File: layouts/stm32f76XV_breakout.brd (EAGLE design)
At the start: 35.6 x 44.5 mm, 52 parts, among them J1 FTSH-105-01-F-DV-K, K1 USB-MICROZX62R-B, K2 MICRO_SD01, Q1 25 MHz, T2 FDC5614P, U3 LMZ21701, U5 NUF2221

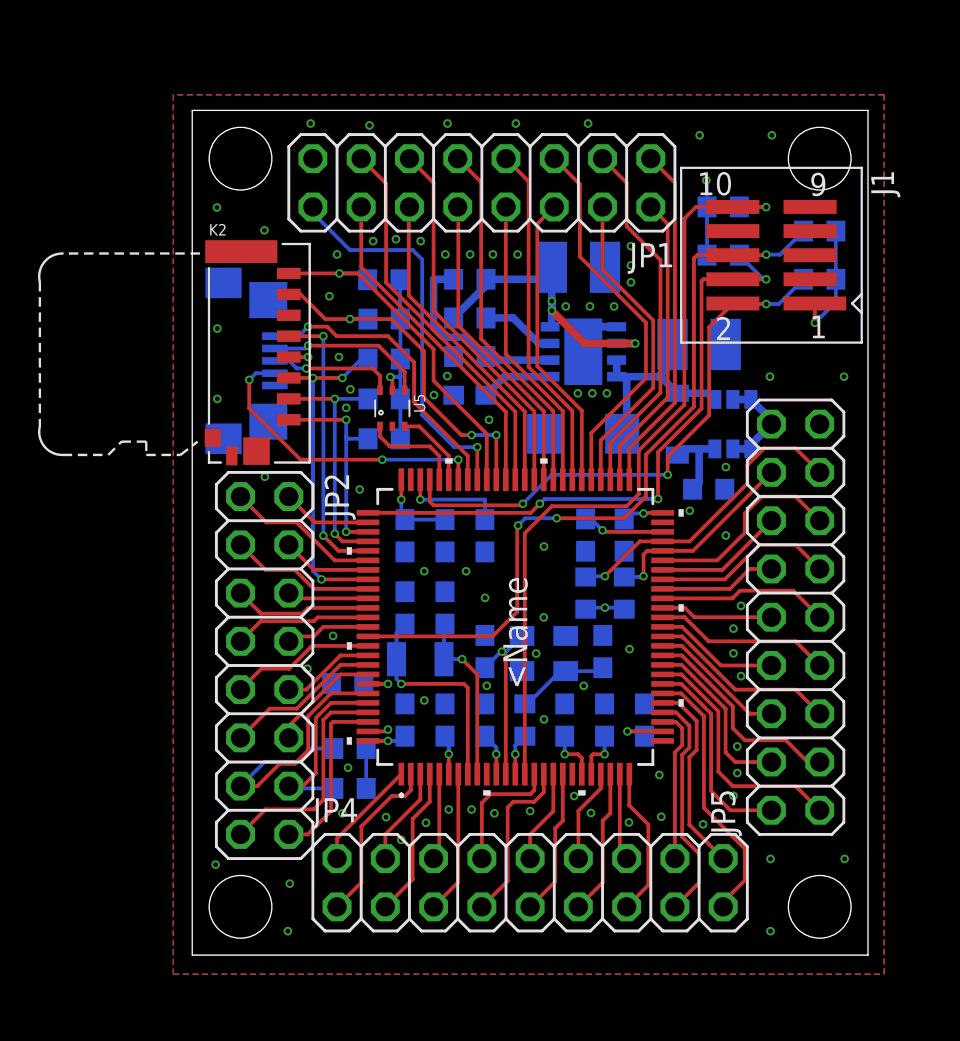
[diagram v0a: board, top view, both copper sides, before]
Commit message: aligned all pinheaders to 2.54mm
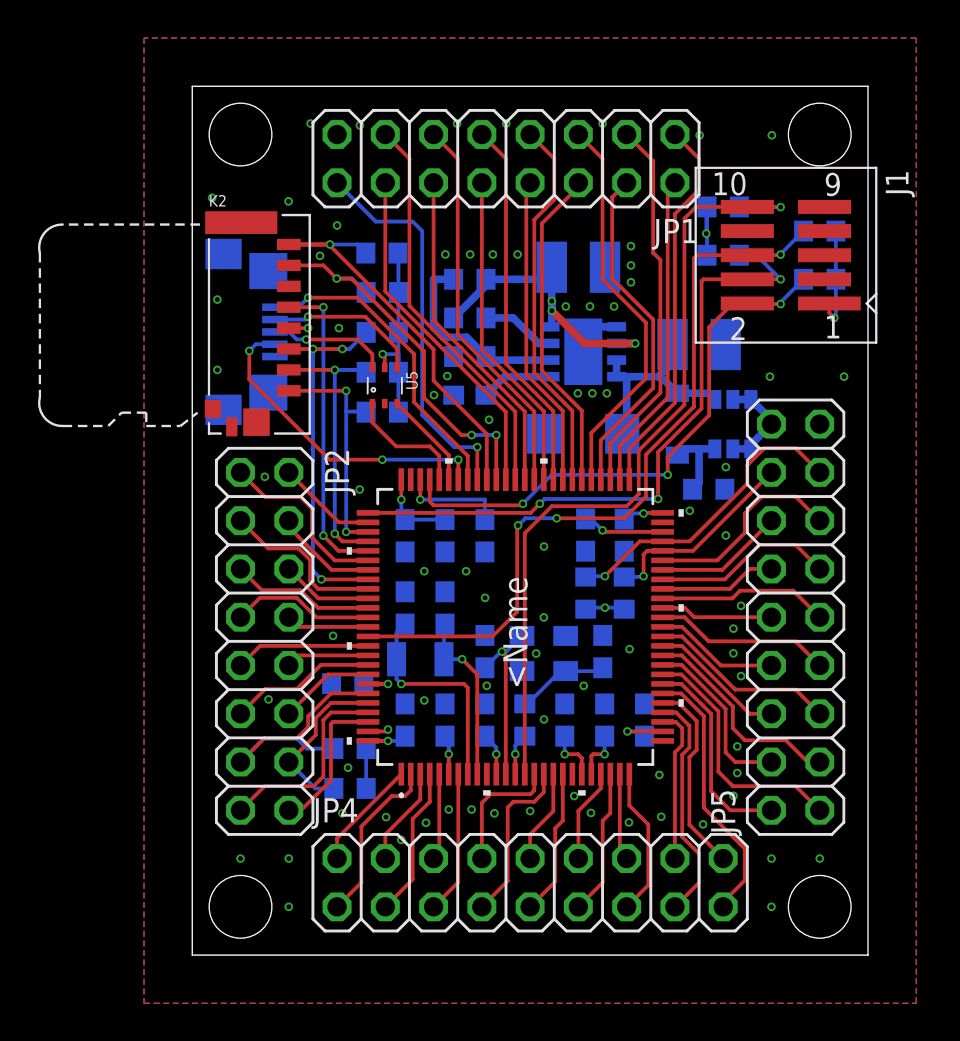
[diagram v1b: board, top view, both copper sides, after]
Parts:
- moved JP1 1.80 mm to (16.5, 41.9)
- moved K1 1.52 mm to (2.00, 32.8)
- moved K2 1.52 mm to (5.08, 33.5)
- moved R4 1.40 mm to (10.0, 30.7)
- moved R5 1.40 mm to (10.0, 32.8)
- moved R22 1.40 mm to (10.0, 28.6)
- moved R6 1.40 mm to (10.0, 34.9)
- moved R7 1.40 mm to (9.98, 36.9)
- moved JP2 1.27 mm to (3.81, 16.5)
- moved U5 1.26 mm to (10.1, 30.0)
- moved J1 0.76 mm to (31.2, 36.8)
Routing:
- net SDIO_D1: track 18.9 -> 22.2 mm
- net SDIO_D0: track 18.7 -> 20.9 mm
- net SPI2_NSS: track 18.4 -> 20.2 mm
- net SWCLK: track 33.3 -> 35.0 mm
- net USART3_CK: track 18.3 -> 19.9 mm
- net USART3_RX: track 15.7 -> 17.3 mm
- net SDIO_CLK: track 15.0 -> 16.5 mm
- net !RESET: track 41.0 -> 42.5 mm
- net UART8_TX: track 9.32 -> 7.84 mm
- net SDIO_D3: track 13.2 -> 14.7 mm
- net CAN1_RX: track 8.10 -> 9.52 mm
- net SDIO_D2: track 11.3 -> 12.7 mm
- net SPI2_MOSI: track 16.6 -> 18.0 mm
- net SDIO_CMD: track 17.8 -> 19.2 mm
- net I2C1_SCL: track 15.5 -> 14.2 mm
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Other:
- board size 35.6 x 44.5 mm -> 35.6 x 45.7 mm

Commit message: added triac driver board
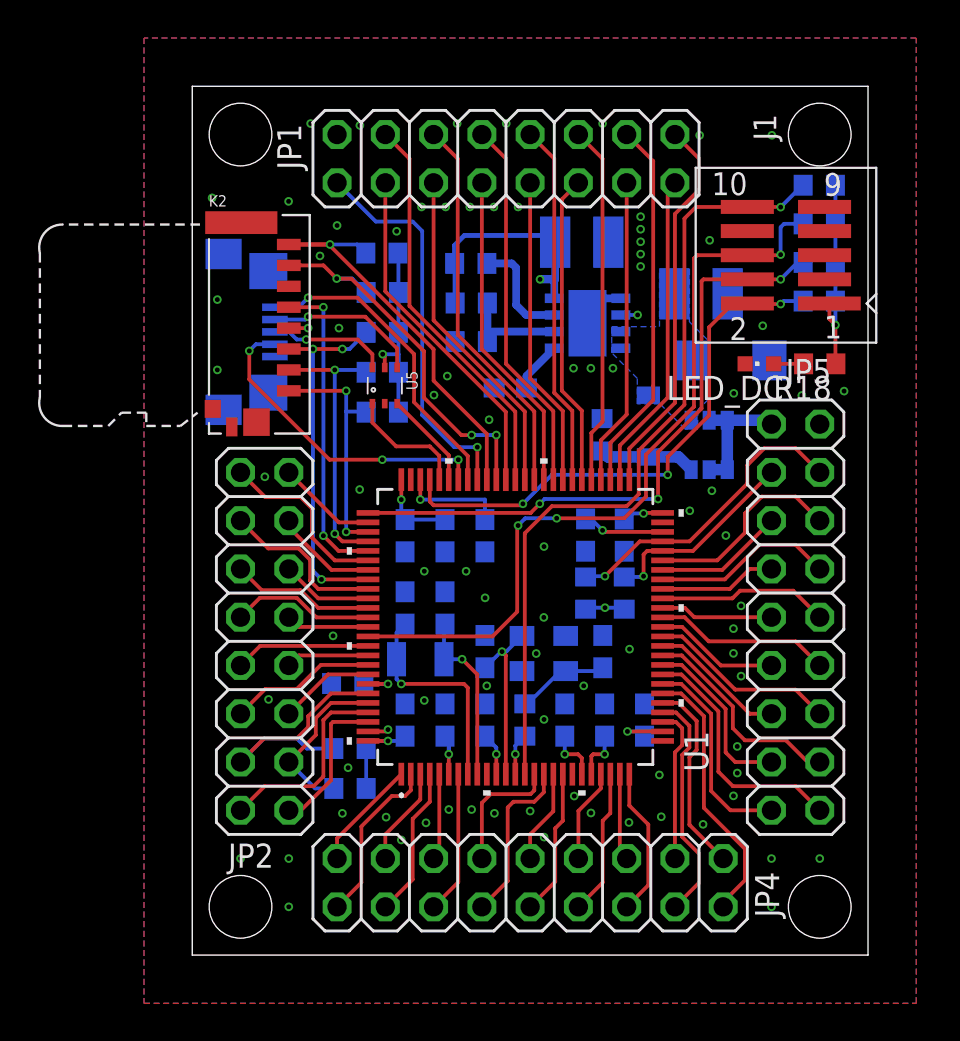
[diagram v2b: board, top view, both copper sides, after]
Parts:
- added LED_DC: (no value), led:CHIPLED_0603
- added R18: 4k7, rcl:R0603
- moved D4 8.66 mm to (28.3, 31.3), turned to 180 degrees
- moved R16 6.30 mm to (21.6, 27.4), turned to 270 degrees
- moved R17 5.18 mm to (33.0, 40.5), turned to 0 degrees
- moved R21 5.07 mm to (33.0, 36.4), turned to 0 degrees
- moved R10 2.87 mm to (14.7, 36.4)
- moved C22 2.67 mm to (26.8, 34.8)
- moved C21 2.17 mm to (16.7, 29.8)
- moved T2 1.66 mm to (27.2, 26.8)
- moved D3 1.53 mm to (24.0, 27.8)
- moved U3 1.52 mm to (20.8, 33.2)
- moved C23 1.33 mm to (20.5, 37.5)
- moved R13 1.25 mm to (14.7, 34.3), turned to 0 degrees
- moved R8 1.14 mm to (33.0, 34.4)
- moved R14 0.79 mm to (14.7, 32.3)
- moved R20 0.38 mm to (33.0, 38.5)
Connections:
- net N$23 renamed LMZ_VIN
- net N$5 renamed LMZ_SS
- net N$7 renamed LMZ_PG
- net N$8 renamed LMZ_FB
- net V_IN renamed SUPPLY
- new net N$5: LED_DC.A, R18.2
- net +3V3: now also R18.1
- net GND: now also LED_DC.C
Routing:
- net LMZ_VIN: track 11.6 -> 0.02 mm
- net LMZ_FB: track 10.8 -> 6.08 mm
- net USART3_TX: track 20.8 -> 18.9 mm
- net LMZ_PG: track 3.93 -> 5.82 mm
- net SPI2_MOSI: track 18.0 -> 16.2 mm
- net SUPPLY: track 5.40 -> 7.03 mm
- net N$5: track 0.00 -> 1.58 mm
- net SWCLK: track 35.0 -> 33.9 mm
- net LMZ_SS: track 3.78 -> 2.70 mm
- net SWO: track 40.3 -> 41.3 mm
- net USART3_CK: track 19.9 -> 19.1 mm
- net +3V3: track 65.2 -> 65.9 mm, vias 16 -> 14
- net N$36: track 4.38 -> 5.10 mm
- net USART3_RX: track 17.3 -> 16.6 mm
- net SWDIO: track 30.1 -> 29.5 mm
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- added copper zone on layer 16, net LMZ_VIN
